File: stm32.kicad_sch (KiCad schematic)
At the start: 17 parts, among them J1 TC2030-IDC, U2 STM32F410CBU6, U3 RT9080-33GJ5

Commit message: adding logo and docs
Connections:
- net VDD: no longer C8.1, U3.5 (VOUT)
- new net: C8.1, U3.5 (VOUT)
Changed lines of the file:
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@@
     (effects (font (size 1.27 1.27)) (justify right))
-  )
-  (hierarchical_label "3V3" (shape input) (at 69.215 54.61 180) (fields_autoplaced)
-    (effects (font (size 1.27 1.27)) (justify right))
-  )
-  (hierarchical_label "3V3" (shape input) (at 76.835 24.13 0) (fields_autoplaced)
-    (effects (font (size 1.27 1.27)) (justify left))
   )
   (hierarchical_label "RX-ASIC" (shape input) (at 92.71 106.045 180) (fields_autoplaced)

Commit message: added BZM2 footprint
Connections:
- net RESET: now also U2.17 (PA7)
- net TRIP: now reaches U2.29 (PA8)
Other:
- note added: "USART1"
- note added: "USART6"
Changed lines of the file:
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@@
+    (stroke (width 0) (type default))
+  )
+  (wire (pts (xy 92.71 93.345) (xy 103.505 93.345))
     (stroke (width 0) (type default))
   )
@@
     (stroke (width 0) (type default))
   )
+  (wire (pts (xy 92.71 95.885) (xy 103.505 95.885))
+    (stroke (width 0) (type default))
+  )
   (wire (pts (xy 73.025 37.465) (xy 66.675 37.465))
     (stroke (width 0) (type default))
@@
   )
   (text "ESP32 3V3 LDO" (at 45.72 40.64 0)
+    (effects (font (size 1.27 1.27)) (justify left bottom))
+  )
+  (text "USART1" (at 73.025 100.33 0)
+    (effects (font (size 1.27 1.27)) (justify left bottom))
+  )
+  (text "USART6" (at 73.025 105.41 0)
     (effects (font (size 1.27 1.27)) (justify left bottom))
   )
@@
     (effects (font (size 1.27 1.27)) (justify right))
   )
+  (hierarchical_label "RESET" (shape output) (at 92.71 93.345 180) (fields_autoplaced)
+    (effects (font (size 1.27 1.27)) (justify right))
+  )
   (hierarchical_label "RX-ESP32" (shape input) (at 92.71 100.965 180) (fields_autoplaced)
     (effects (font (size 1.27 1.27)) (justify right))
@@
     (effects (font (size 1.27 1.27)) (justify right))
   )
+  (hierarchical_label "TRIP" (shape input) (at 92.71 95.885 180) (fields_autoplaced)
+    (effects (font (size 1.27 1.27)) (justify right))
+  )

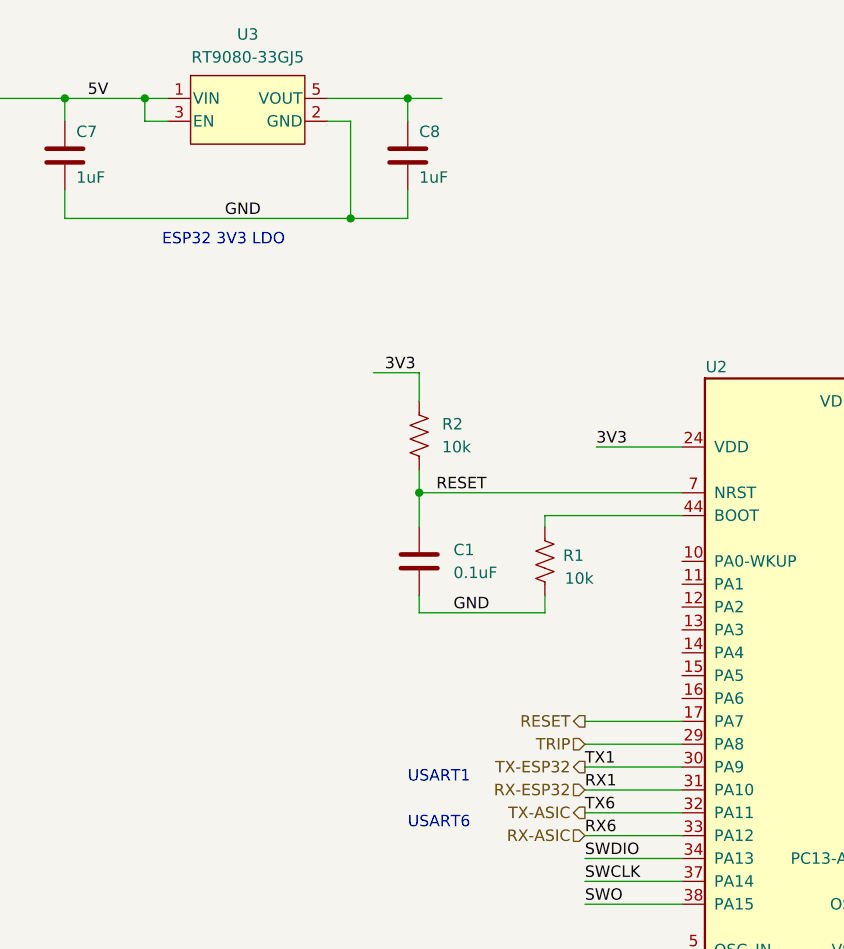
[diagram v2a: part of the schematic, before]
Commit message: migrated over lots of bitaxe parts to blockaxe
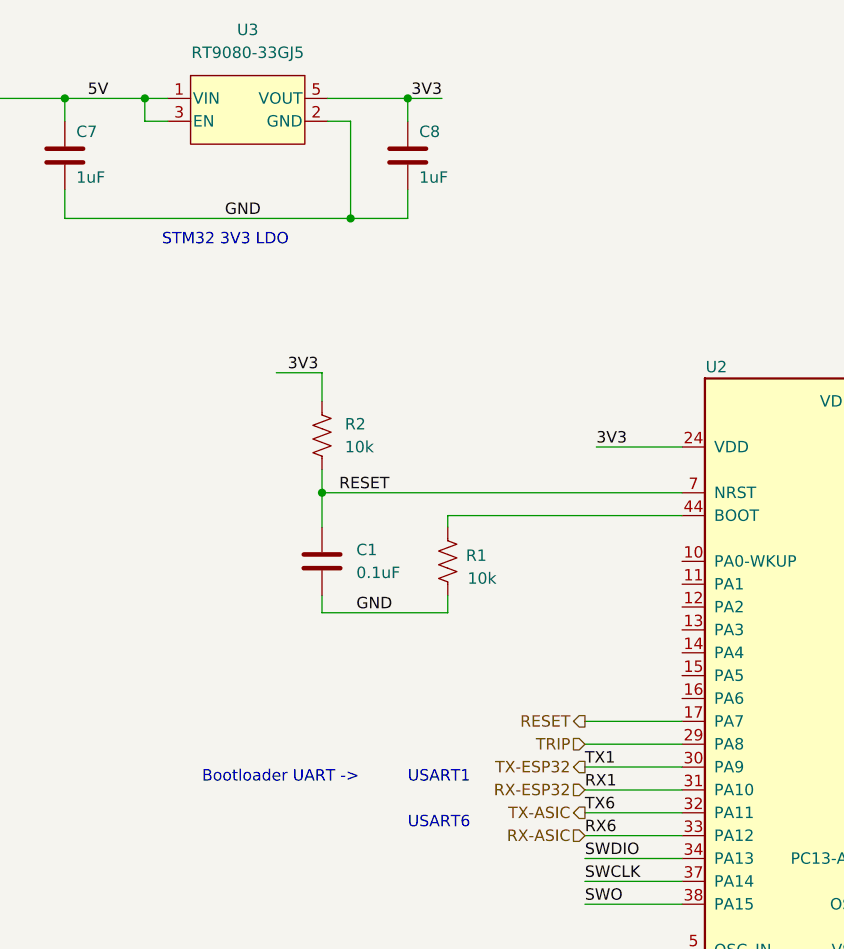
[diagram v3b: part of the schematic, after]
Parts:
- J1: footprint Connector:Tag-Connect_TC2030-IDC-NL_2x03_P1.27mm_Vertical -> blockaxe:Tag-Connect_TC2030-IDC-NL_2x03_P1.27mm_Vertical; symbol bitaxe:TC2030-IDC-NL -> blockaxe:TC2030-IDC-NL
- U3: footprint bitaxe:RT9080-33GJ5 -> blockaxe:RT9080-33GJ5; symbol bitaxe:RT9080-33GJ5 -> blockaxe:RT9080-33GJ5
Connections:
- net VDD: now also C8.1, U3.5 (VOUT)
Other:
- note added: "Bootloader UART ->"
- note added: "STM32 3V3 LDO"
- note removed: "ESP32 3V3 LDO"
- moved on the sheet: C1, R1, R2
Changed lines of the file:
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@@
   (junction (at 140.335 118.745) (diameter 0) (color 0 0 0 0)
   )
-  (junction (at 74.295 67.945) (diameter 0) (color 0 0 0 0)
+  (junction (at 63.5 67.945) (diameter 0) (color 0 0 0 0)
   )
   (junction (at 73.025 24.13) (diameter 0) (color 0 0 0 0)
@@
     (stroke (width 0) (type default))
   )
-  (wire (pts (xy 74.295 65.405) (xy 74.295 67.945))
+  (wire (pts (xy 63.5 65.405) (xy 63.5 67.945))
     (stroke (width 0) (type default))
   )
@@
     (stroke (width 0) (type default))
   )
-  (wire (pts (xy 74.295 67.945) (xy 74.295 71.755))
+  (wire (pts (xy 63.5 67.945) (xy 63.5 71.755))
     (stroke (width 0) (type default))
   )
@@
     (stroke (width 0) (type default))
   )
-  (wire (pts (xy 74.295 79.375) (xy 74.295 81.28))
+  (wire (pts (xy 63.5 79.375) (xy 63.5 81.28))
     (stroke (width 0) (type default))
   )
@@
     (stroke (width 0) (type default))
   )
-  (wire (pts (xy 74.295 54.61) (xy 74.295 57.785))
+  (wire (pts (xy 63.5 54.61) (xy 63.5 57.785))
     (stroke (width 0) (type default))
   )
@@
     (stroke (width 0) (type default))
   )
-  (wire (pts (xy 69.215 54.61) (xy 74.295 54.61))
+  (wire (pts (xy 58.42 54.61) (xy 63.5 54.61))
     (stroke (width 0) (type default))
   )
@@
     (stroke (width 0) (type default))
   )
-  (wire (pts (xy 88.265 79.375) (xy 88.265 81.28))
+  (wire (pts (xy 77.47 79.375) (xy 77.47 81.28))
     (stroke (width 0) (type default))
   )
@@
     (stroke (width 0) (type default))
   )
-  (wire (pts (xy 88.265 70.485) (xy 88.265 71.755))
+  (wire (pts (xy 77.47 70.485) (xy 77.47 71.755))
     (stroke (width 0) (type default))
   )
@@
     (stroke (width 0) (type default))
   )
-  (wire (pts (xy 74.295 81.28) (xy 88.265 81.28))
+  (wire (pts (xy 63.5 81.28) (xy 77.47 81.28))
     (stroke (width 0) (type default))
   )
@@
     (stroke (width 0) (type default))
   )
-  (wire (pts (xy 103.505 70.485) (xy 88.265 70.485))
-    (stroke (width 0) (type default))
-  )
-  (wire (pts (xy 103.505 67.945) (xy 74.295 67.945))
+  (wire (pts (xy 103.505 70.485) (xy 77.47 70.485))
+    (stroke (width 0) (type default))
+  )
+  (wire (pts (xy 103.505 67.945) (xy 63.5 67.945))
     (stroke (width 0) (type default))
   )
@@
     (stroke (width 0) (type default))
   )
-  (text "ESP32 3V3 LDO" (at 45.72 40.64 0)
+  (text "Bootloader UART ->" (at 50.165 100.33 0)
+    (effects (font (size 1.27 1.27)) (justify left bottom))
+  )
+  (text "STM32 3V3 LDO" (at 45.72 40.64 0)
     (effects (font (size 1.27 1.27)) (justify left bottom))
   )
@@
     (effects (font (size 1.27 1.27)) (justify left bottom))
   )
-  (label "GND" (at 78.105 81.28 0) (fields_autoplaced)
+  (label "GND" (at 67.31 81.28 0) (fields_autoplaced)
     (effects (font (size 1.27 1.27)) (justify left bottom))
   )
@@
     (effects (font (size 1.27 1.27)) (justify left bottom))
   )
-  (label "RESET" (at 76.2 67.945 0) (fields_autoplaced)
-    (effects (font (size 1.27 1.27)) (justify left bottom))
+  (label "RESET" (at 65.405 67.945 0) (fields_autoplaced)
+    (effects (font (size 1.27 1.27)) (justify left bottom))
+  )
+  (label "3V3" (at 76.835 24.13 180) (fields_autoplaced)
+    (effects (font (size 1.27 1.27)) (justify right bottom))
   )
   (label "3V3" (at 143.51 60.325 180) (fields_autoplaced)
@@
     (effects (font (size 1.27 1.27)) (justify left bottom))
   )
-  (label "3V3" (at 70.485 54.61 0) (fields_autoplaced)
+  (label "3V3" (at 59.69 54.61 0) (fields_autoplaced)
     (effects (font (size 1.27 1.27)) (justify left bottom))
   )
@@
     )
   )
-  (symbol (lib_id "bitaxe:TC2030-IDC-NL") (at 195.58 116.84 0) (unit 1)
+  (symbol (lib_id "blockaxe:TC2030-IDC-NL") (at 195.58 116.84 0) (unit 1)
     (in_bom yes) (on_board yes) (dnp no) (fields_autoplaced)
     (property "Reference" "J1" (at 195.58 104.14 0)
@@
       (effects (font (size 1.27 1.27)))
     )
-    (property "Footprint" "Connector:Tag-Connect_TC2030-IDC-NL_2x03_P1.27mm_Vertical" (at 194.31 116.84 0)
+    (property "Footprint" "blockaxe:Tag-Connect_TC2030-IDC-NL_2x03_P1.27mm_Vertical" (at 194.31 116.84 0)
       (effects (font (size 1.27 1.27)) hide)
     )
@@
     )
   )
-  (symbol (lib_id "Device:R_US") (at 74.295 61.595 180) (unit 1)
+  (symbol (lib_id "Device:R_US") (at 63.5 61.595 180) (unit 1)
     (in_bom yes) (on_board yes) (dnp no) (fields_autoplaced)
-    (property "Reference" "R2" (at 76.835 60.325 0)
+    (property "Reference" "R2" (at 66.04 60.325 0)
       (effects (font (size 1.27 1.27)) (justify right))
     )
-    (property "Value" "10k" (at 76.835 62.865 0)
+    (property "Value" "10k" (at 66.04 62.865 0)
       (effects (font (size 1.27 1.27)) (justify right))
     )
-    (property "Footprint" "" (at 73.279 61.341 90)
-      (effects (font (size 1.27 1.27)) hide)
-    )
-    (property "Datasheet" "~" (at 74.295 61.595 0)
+    (property "Footprint" "" (at 62.484 61.341 90)
+      (effects (font (size 1.27 1.27)) hide)
+    )
+    (property "Datasheet" "~" (at 63.5 61.595 0)
       (effects (font (size 1.27 1.27)) hide)
     )
@@
     )
   )
-  (symbol (lib_id "bitaxe:RT9080-33GJ5") (at 55.245 25.4 0) (unit 1)
+  (symbol (lib_id "blockaxe:RT9080-33GJ5") (at 55.245 25.4 0) (unit 1)
     (in_bom yes) (on_board yes) (dnp no) (fields_autoplaced)
-    (property "Reference" "U3" (at 55.245 17.018 0)
-      (effects (font (size 1.27 1.27)))
-    )
-    (property "Value" "RT9080-33GJ5" (at 55.245 19.558 0)
-      (effects (font (size 1.27 1.27)))
-    )
-    (property "Footprint" "bitaxe:RT9080-33GJ5" (at 104.775 7.62 0)
+    (property "Reference" "U3" (at 55.245 16.51 0)
+      (effects (font (size 1.27 1.27)))
+    )
+    (property "Value" "RT9080-33GJ5" (at 55.245 19.05 0)
+      (effects (font (size 1.27 1.27)))
+    )
+    (property "Footprint" "blockaxe:RT9080-33GJ5" (at 104.775 7.62 0)
       (effects (font (size 1.524 1.524)) hide)
     )
@@
     )
   )
-  (symbol (lib_id "Device:R_US") (at 88.265 75.565 180) (unit 1)
+  (symbol (lib_id "Device:R_US") (at 77.47 75.565 180) (unit 1)
     (in_bom yes) (on_board yes) (dnp no)
-    (property "Reference" "R1" (at 91.44 74.93 0)
-      (effects (font (size 1.27 1.27)))
-    )
-    (property "Value" "10k" (at 92.075 77.47 0)
-      (effects (font (size 1.27 1.27)))
-    )
-    (property "Footprint" "" (at 87.249 75.311 90)
-      (effects (font (size 1.27 1.27)) hide)
-    )
-    (property "Datasheet" "~" (at 88.265 75.565 0)
+    (property "Reference" "R1" (at 80.645 74.93 0)
+      (effects (font (size 1.27 1.27)))
+    )
+    (property "Value" "10k" (at 81.28 77.47 0)
+      (effects (font (size 1.27 1.27)))
+    )
+    (property "Footprint" "" (at 76.454 75.311 90)
+      (effects (font (size 1.27 1.27)) hide)
+    )
+    (property "Datasheet" "~" (at 77.47 75.565 0)
       (effects (font (size 1.27 1.27)) hide)
     )
@@
     )
   )
-  (symbol (lib_id "Device:C") (at 74.295 75.565 0) (unit 1)
+  (symbol (lib_id "Device:C") (at 63.5 75.565 0) (unit 1)
     (in_bom yes) (on_board yes) (dnp no) (fields_autoplaced)
-    (property "Reference" "C1" (at 78.105 74.295 0)
-      (effects (font (size 1.27 1.27)) (justify left))
-    )
-    (property "Value" "0.1uF" (at 78.105 76.835 0)
-      (effects (font (size 1.27 1.27)) (justify left))
-    )
-    (property "Footprint" "" (at 75.2602 79.375 0)
-      (effects (font (size 1.27 1.27)) hide)
-    )
-    (property "Datasheet" "~" (at 74.295 75.565 0)
-      (effects (font (size 1.27 1.27)) hide)
-    )
+    (property "Reference" "C1" (at 67.31 74.295 0)
+      (effects (font (size 1.27 1.27)) (justify left))
+    )
+    (property "Value" "0.1uF" (at 67.31 76.835 0)
+      (effects (font (size 1.27 1.27)) (justify left))
+    )
+    (property "Footprint" "" (at 64.4652 79.375 0)
+      (effects (font (size 1.27 1.27)) hide)
+    )
+    (property "Datasheet" "~" (at 63.5 75.565 0)
+      (effects (font (size 1.27 1.27)) hide)
+    )

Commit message: all the footprints are in?
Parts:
- C1, C2, C3, C4, C5, C6: footprint (none) -> Capacitor_SMD:C_0402_1005Metric
- R1, R2: footprint (none) -> Resistor_SMD:R_0402_1005Metric
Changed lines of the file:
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@@
       (effects (font (size 1.27 1.27)) (justify left))
     )
-    (property "Footprint" "" (at 190.1952 66.04 0)
+    (property "Footprint" "Capacitor_SMD:C_0402_1005Metric" (at 190.1952 66.04 0)
       (effects (font (size 1.27 1.27)) hide)
     )
@@
       (effects (font (size 1.27 1.27)) (justify left))
     )
-    (property "Footprint" "" (at 146.3802 73.025 0)
+    (property "Footprint" "Capacitor_SMD:C_0402_1005Metric" (at 146.3802 73.025 0)
       (effects (font (size 1.27 1.27)) hide)
     )
@@
       (effects (font (size 1.27 1.27)) (justify left))
     )
-    (property "Footprint" "" (at 176.2252 66.04 0)
+    (property "Footprint" "Capacitor_SMD:C_0402_1005Metric" (at 176.2252 66.04 0)
       (effects (font (size 1.27 1.27)) hide)
     )
@@
       (effects (font (size 1.27 1.27)) (justify left))
     )
-    (property "Footprint" "" (at 204.1652 66.04 0)
+    (property "Footprint" "Capacitor_SMD:C_0402_1005Metric" (at 204.1652 66.04 0)
       (effects (font (size 1.27 1.27)) hide)
     )
@@
       (effects (font (size 1.27 1.27)) (justify right))
     )
-    (property "Footprint" "" (at 62.484 61.341 90)
+    (property "Footprint" "Resistor_SMD:R_0402_1005Metric" (at 62.484 61.341 90)
       (effects (font (size 1.27 1.27)) hide)
     )
@@
       (effects (font (size 1.27 1.27)))
     )
-    (property "Footprint" "" (at 76.454 75.311 90)
+    (property "Footprint" "Resistor_SMD:R_0402_1005Metric" (at 76.454 75.311 90)
       (effects (font (size 1.27 1.27)) hide)
     )
@@
       (effects (font (size 1.27 1.27)) (justify left))
     )
-    (property "Footprint" "" (at 64.4652 79.375 0)
+    (property "Footprint" "Capacitor_SMD:C_0402_1005Metric" (at 64.4652 79.375 0)
       (effects (font (size 1.27 1.27)) hide)
     )
@@
       (effects (font (size 1.27 1.27)) (justify left))
     )
-    (property "Footprint" "" (at 216.8652 66.04 0)
-      (effects (font (size 1.27 1.27)) hide)
-    )
+    (property "Footprint" "Capacitor_SMD:C_0402_1005Metric" (at 216.8652 66.04 0)
+      (effects (font (size 1.27 1.27)) hide)
+    )
